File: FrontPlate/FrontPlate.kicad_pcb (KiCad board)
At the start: 2 copper layers, 92.5 x 60.9 mm, 15 parts

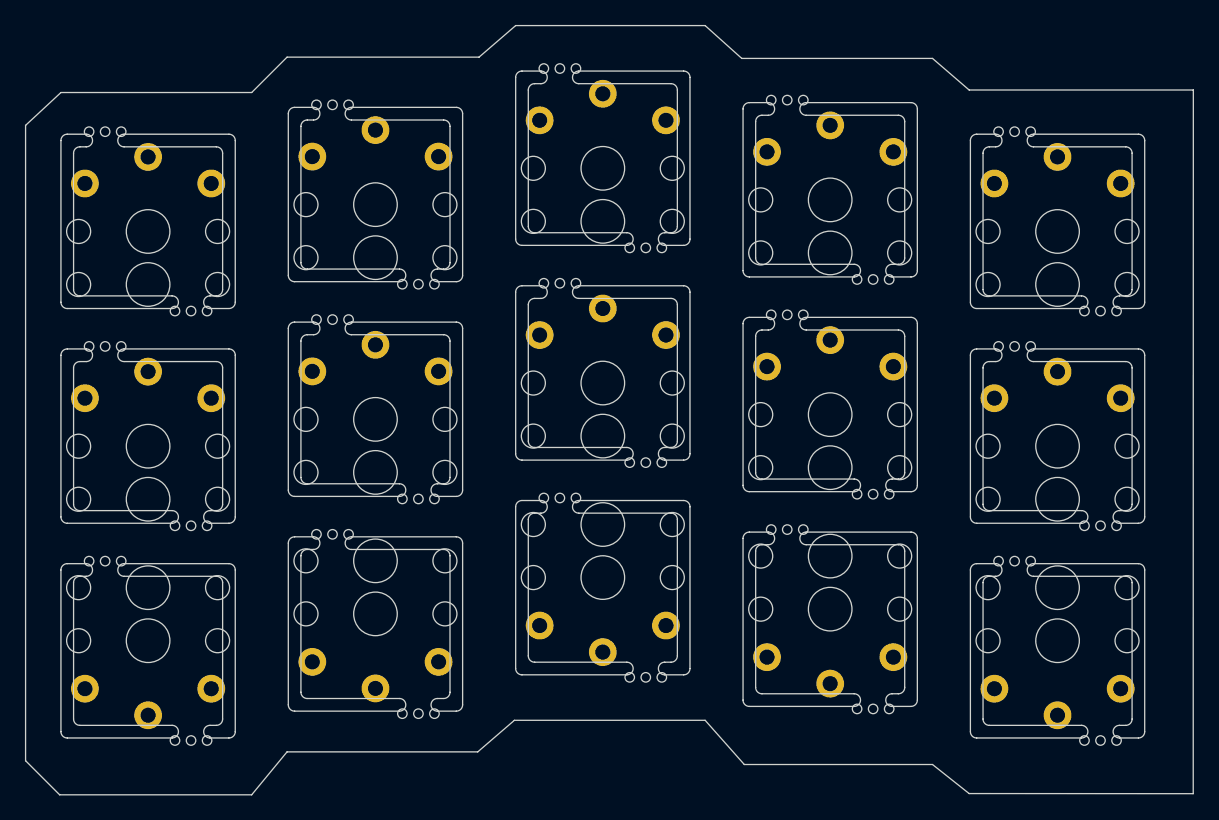
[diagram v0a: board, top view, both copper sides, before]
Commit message: better front plate
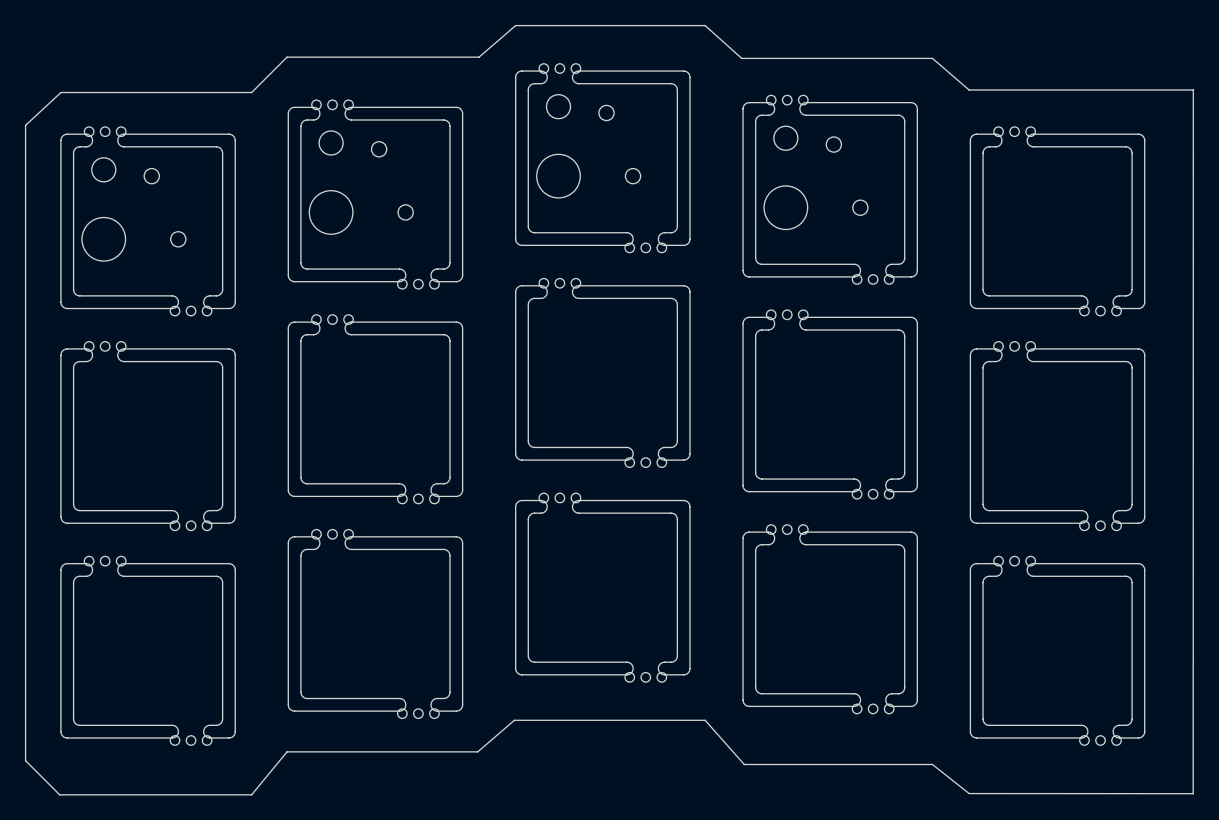
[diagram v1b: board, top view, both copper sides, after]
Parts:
- S1, S2, S3, S4: footprint keyswitches:PLATE_choc_footprint -> Footprints:PLATE_choc_footprint_exp
- S10, S11, S12, S13, S14, S15, S5, S6, S7, S8, S9: footprint keyswitches:PLATE_choc_footprint -> Footprints:PLATE_choc
